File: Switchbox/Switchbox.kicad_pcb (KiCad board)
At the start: 2 copper layers, 90 x 68 mm, 42 parts, among them J1 USB-C_connector, SW1 SW_SPDT, SW2 SW_SPDT, SW3 SW_SPDT, SW4 SW_SPDT, SW5 SW_SPST_LED, SW6 SW_SPDT_BOX, U2 AP63203WU

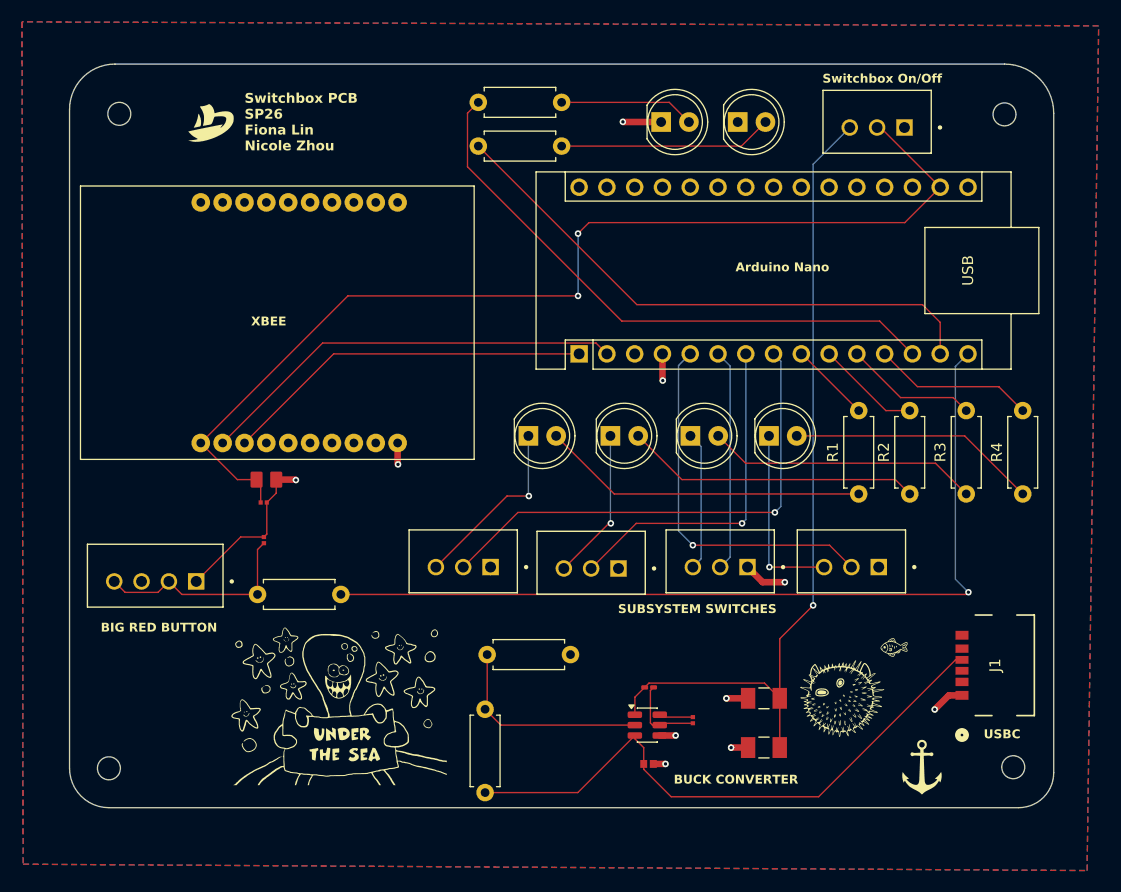
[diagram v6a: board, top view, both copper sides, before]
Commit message: changed resistors, LEDs, traces, some labels
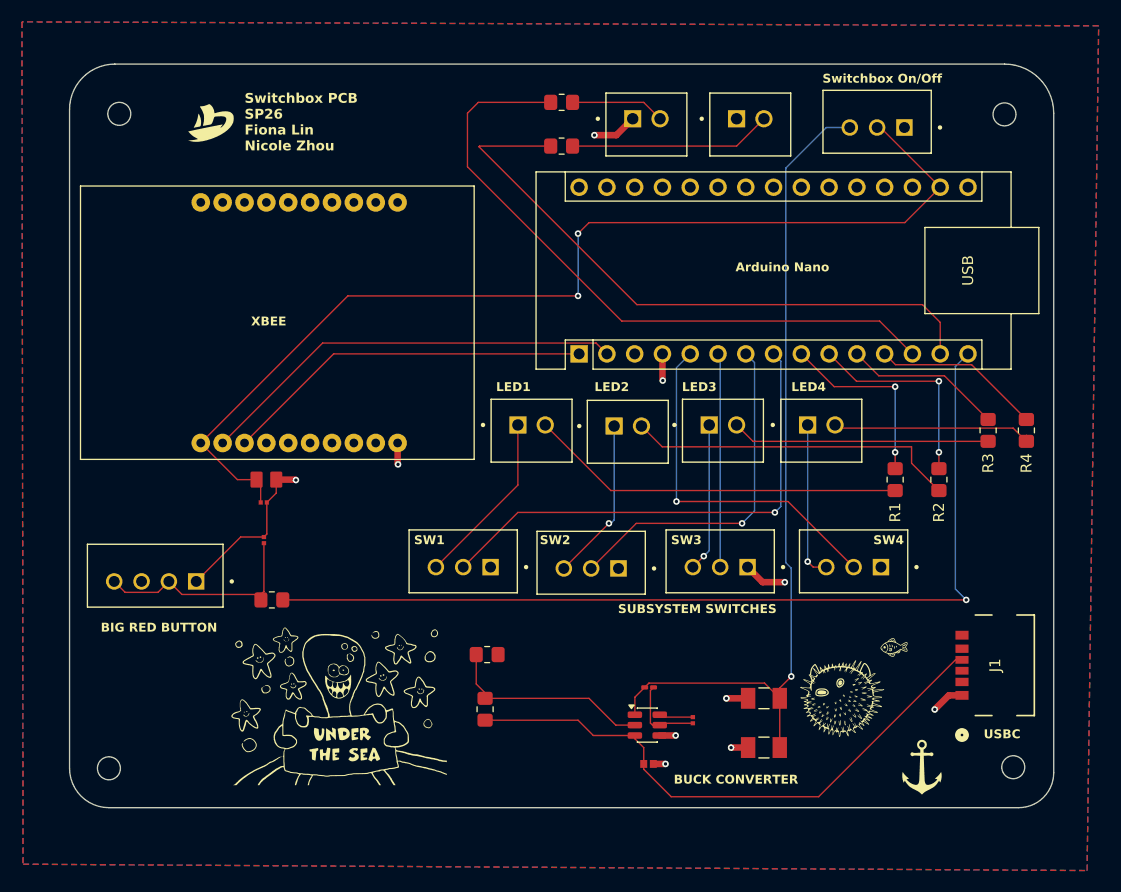
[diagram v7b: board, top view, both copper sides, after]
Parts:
- D1, D2, D3, D4, D5, D6: footprint LED_THT:LED_D5.0mm -> switchbox_footprints:2_pin_header
- R1, R2, R3, R3a1, R3b1, R4, R5, R6, R7: footprint Resistor_THT:R_Axial_DIN0207_L6.3mm_D2.5mm_P7.62mm_Horizontal -> Resistor_SMD:R_0805_2012Metric_Pad1.20x1.40mm_HandSolder
- moved R7 6.33 mm to (121.5, 134.0)
- moved R3 6.14 mm to (187.0, 118.5)
- moved R4 5.82 mm to (190.5, 118.5)
- moved D4 5.31 mm to (172.2, 118.2), turned to 180 degrees
- moved R1 3.58 mm to (178.5, 123.0)
- moved D3 3.52 mm to (163.2, 118.2), turned to 180 degrees
- moved R2 2.97 mm to (182.5, 123.0)
- moved D2 2.17 mm to (154.5, 118.2), turned to 180 degrees
- moved D6 1.61 mm to (165.7, 90.2), turned to 180 degrees
- moved D1 1.13 mm to (145.7, 118.2), turned to 180 degrees
- moved D5 0.91 mm to (156.2, 90.2), turned to 180 degrees
- moved SW4 0.20 mm to (174.5, 130.9)
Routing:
- net LED1_PWR: track 7.40 -> 17.4 mm, vias 0 -> 2
- net LED2_PWR: track 9.52 -> 19.1 mm, vias 0 -> 2
- net LED5_PWR: track 54.1 -> 60.7 mm
- net LED6_PWR: track 51.8 -> 58.3 mm
- net BUTTON: track 80.2 -> 85.9 mm
- net Net-(D1-A): track 29.9 -> 34.5 mm
- net Net-(D4-A): track 22.9 -> 18.7 mm
- net Net-(D5-A): track 12.4 -> 8.62 mm
- net Net-(D2-A): track 27.0 -> 30.5 mm
- net Net-(D4-K): track 17.0 -> 14.2 mm
- net LED3_PWR: track 12.1 -> 14.5 mm
- net 3.3VBuck: track 75.3 -> 77.0 mm
- net Sys_Vin: track 54.6 -> 53.0 mm
- net Net-(D3-A): track 24.9 -> 23.6 mm
- net LED4_STATE: track 33.8 -> 32.7 mm
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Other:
- board text added: "680"
- board text added: "LED1"
- board text added: "LED2"
- board text added: "LED3"
- board text added: "LED4"
- board text added: "SW1"
- board text added: "SW2"
- board text added: "SW3"
- board text added: "SW4"

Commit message: uploaded jlc board settings, minor change to buck
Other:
- copper layers 2 -> 4
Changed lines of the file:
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@@
 	(generator_version "9.0")
 	(general
-		(thickness 1.6)
+		(thickness 1.600198)
 		(legacy_teardrops no)
 	)
 	(paper "A4")
 	(layers
-		(0 "F.Cu" signal)
-		(2 "B.Cu" signal)
-		(9 "F.Adhes" user "F.Adhesive")
-		(11 "B.Adhes" user "B.Adhesive")
+		(0 "F.Cu" signal "Front")
+		(4 "In1.Cu" signal)
+		(6 "In2.Cu" signal)
+		(2 "B.Cu" signal "Back")
 		(13 "F.Paste" user)
 		(15 "B.Paste" user)
-		(5 "F.SilkS" user "F.Silkscreen")
-		(7 "B.SilkS" user "B.Silkscreen")
+		(5 "F.SilkS" user)
+		(7 "B.SilkS" user)
 		(1 "F.Mask" user)
 		(3 "B.Mask" user)
-		(17 "Dwgs.User" user "User.Drawings")
-		(19 "Cmts.User" user "User.Comments")
-		(21 "Eco1.User" user "User.Eco1")
-		(23 "Eco2.User" user "User.Eco2")
 		(25 "Edge.Cuts" user)
 		(27 "Margin" user)
-		(31 "F.CrtYd" user "F.Courtyard")
-		(29 "B.CrtYd" user "B.Courtyard")
+		(31 "F.CrtYd" user)
+		(29 "B.CrtYd" user)
 		(35 "F.Fab" user)
-		(33 "B.Fab" user)
-		(39 "User.1" user)
-		(41 "User.2" user)
-		(43 "User.3" user)
-		(45 "User.4" user)
 	)
 	(setup
+		(stackup
+			(layer "F.SilkS"
+				(type "Top Silk Screen")
+			)
+			(layer "F.Paste"
+				(type "Top Solder Paste")
+			)
+			(layer "F.Mask"
+				(type "Top Solder Mask")
+				(thickness 0.01)
+			)
+			(layer "F.Cu"
+				(type "copper")
+				(thickness 0.035)
+			)
+			(layer "dielectric 1"
+				(type "core")
+				(thickness 0.480066)
+				(material "FR4")
+				(epsilon_r 4.5)
+				(loss_tangent 0.02)
+			)
+			(layer "In1.Cu"
+				(type "copper")
+				(thickness 0.035)
+			)
+			(layer "dielectric 2"
+				(type "prepreg")
+				(thickness 0.480066)
+				(material "FR4")
+				(epsilon_r 4.5)
+				(loss_tangent 0.02)
+			)
+			(layer "In2.Cu"
+				(type "copper")
+				(thickness 0.035)
+			)
+			(layer "dielectric 3"
+				(type "core")
+				(thickness 0.480066)
+				(material "FR4")
+				(epsilon_r 4.5)
+				(loss_tangent 0.02)
+			)
+			(layer "B.Cu"
+				(type "copper")
+				(thickness 0.035)
+			)
+			(layer "B.Mask"
+				(type "Bottom Solder Mask")
+				(thickness 0.01)
+			)
+			(layer "B.Paste"
+				(type "Bottom Solder Paste")
+			)
+			(layer "B.SilkS"
+				(type "Bottom Silk Screen")
+			)
+			(copper_finish "None")
+			(dielectric_constraints no)
+		)
 		(pad_to_mask_clearance 0)
+		(solder_mask_min_width 0.12)
 		(allow_soldermask_bridges_in_footprints no)
 		(tenting front back)
@@
 			(net 42 "Sys_Vin")
 			(pintype "passive")
-			(solder_mask_margin 0.102)
+			(solder_mask_margin 0)
 		)
 		(pad "2" smd rect
@@
 			(net 6 "GND")
 			(pintype "passive")
-			(solder_mask_margin 0.102)
+			(solder_mask_margin 0)
 		)
 		(embedded_fonts no)
@@
 		(min_thickness 0.25)
 		(filled_areas_thickness no)
-		(fill
+		(fill yes
 			(thermal_gap 0.5)
 			(thermal_bridge_width 0.5)
